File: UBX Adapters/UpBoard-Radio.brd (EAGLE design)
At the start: 32 x 36 mm, 2 parts

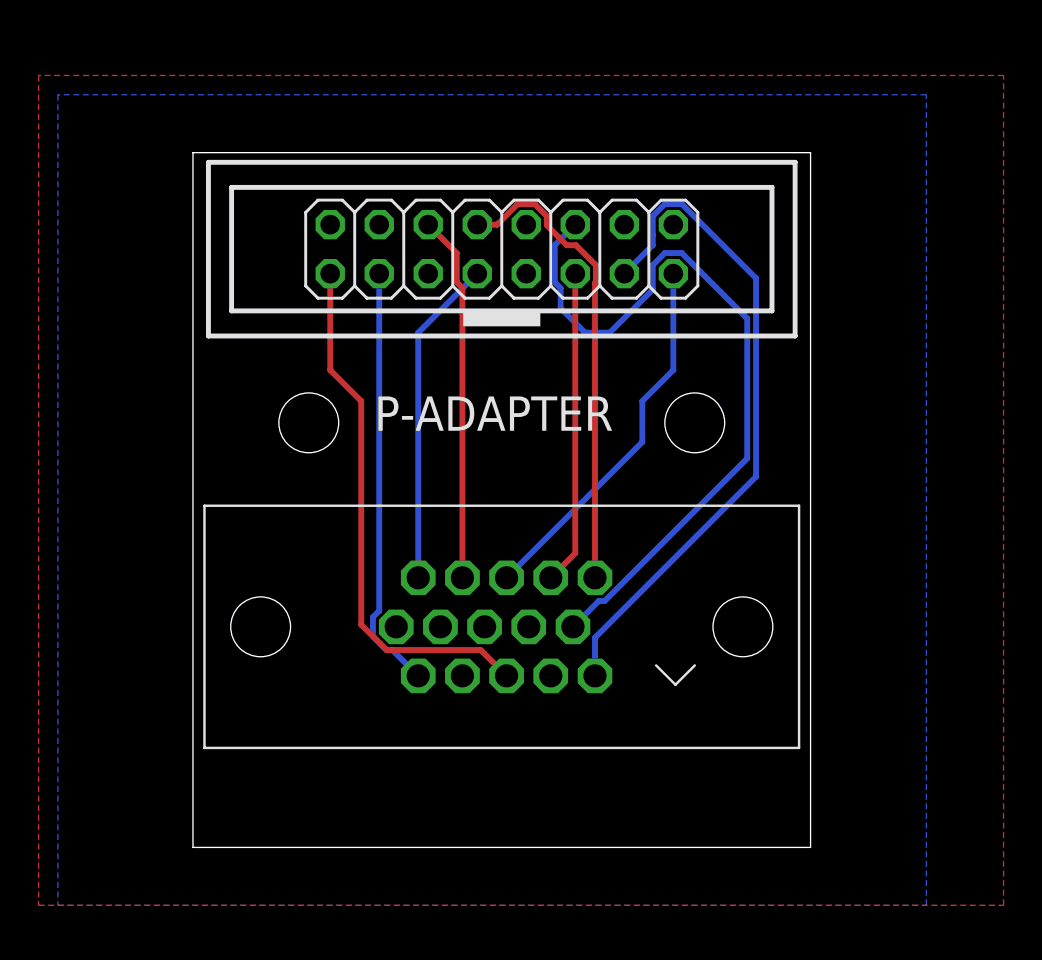
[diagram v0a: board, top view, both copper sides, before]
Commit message: created and finished upboard radio adapter
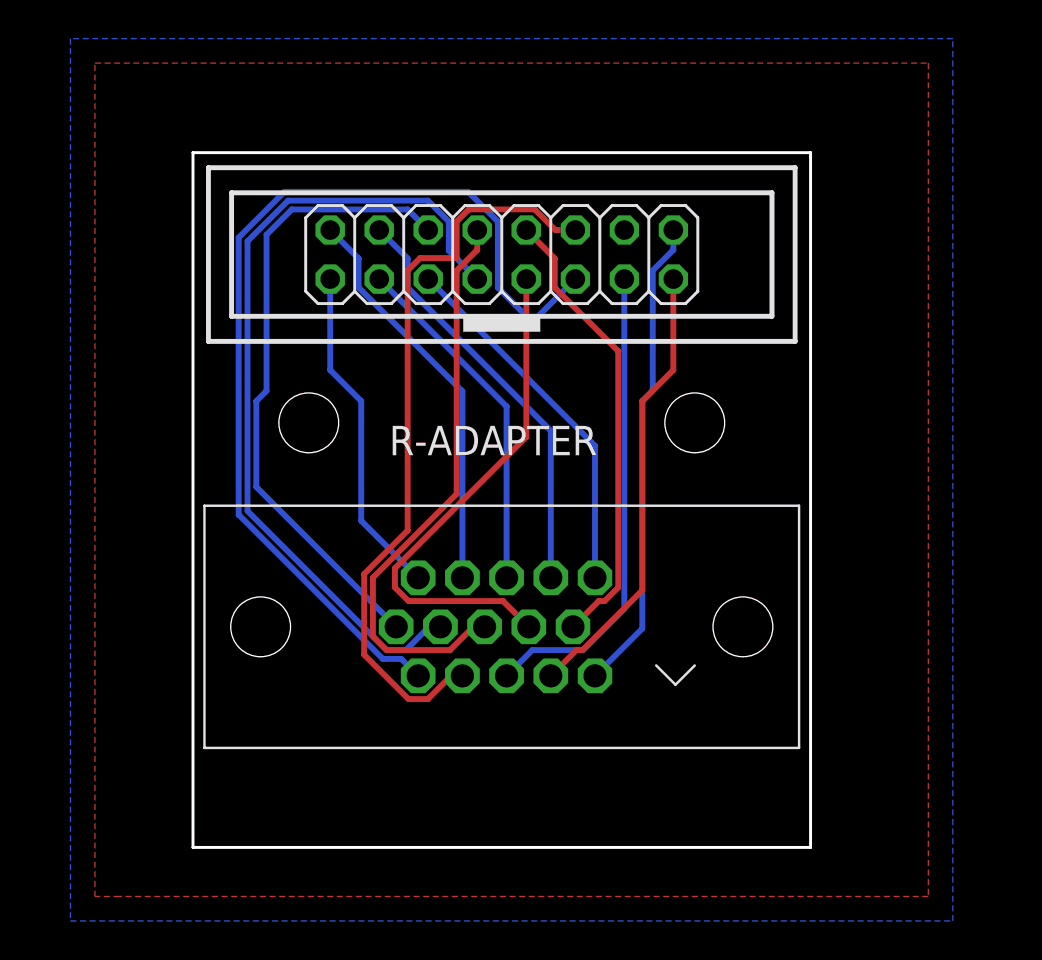
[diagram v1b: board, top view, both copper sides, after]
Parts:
- U$1: value 16POS_RIBBON -> 15POSD-SUBSLDR; device CPSS_CONNECTOR:2X08 -> CPSS_CONNECTOR:15POS-DSUBSLDR
- U$2: value 15POSD-SUBSLDR -> 16POS_RIBBON; device CPSS_CONNECTOR:15POS-DSUBSLDR -> CPSS_CONNECTOR:2X08
- moved U$1 19.6 mm to (16.0, 11.4)
- moved U$2 19.3 mm to (16.0, 30.7)
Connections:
- removed net BUSY: U$1.15, U$2.3
- removed net CONVST: U$1.13, U$2.15
- removed net CS: U$1.11, U$2.4
- removed net RESET: U$1.12, U$2.10
- new net RX: U$1.11, U$2.11
- new net RXS0: U$1.4, U$2.4
- new net SCL: U$1.10, U$2.10
- new net SDA: U$1.9, U$2.9
- new net TX: U$1.12, U$2.12
- new net TXS0: U$1.5, U$2.5
- new net XBEEATTN: U$1.14, U$2.15
- new net XBEECS: U$1.15, U$2.16
- new net XBEERESET: U$1.13, U$2.13
- net 3.3V: now also U$2.1; no longer U$2.13
- net GND: now also U$2.2; no longer U$2.12
- net HV: now also U$2.3; no longer U$2.11
- net MISO: now also U$2.6; no longer U$2.2
- net MOSI: now also U$2.7; no longer U$2.1
- net SCK: now also U$2.8; no longer U$2.5
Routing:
- net RX: track 0.00 -> 51.3 mm
- net TX: track 0.00 -> 38.9 mm
- net RESET: track 38.8 -> 0.00 mm
- net CONVST: track 34.9 -> 0.00 mm
- net SDA: track 0.00 -> 26.6 mm
- net MOSI: track 17.0 -> 42.8 mm
- net XBEECS: track 0.00 -> 24.8 mm
- net XBEERESET: track 0.00 -> 24.6 mm
- net SCL: track 0.00 -> 23.7 mm
- net XBEEATTN: track 0.00 -> 23.4 mm
- net RXS0: track 0.00 -> 21.7 mm
- net GND: track 0.00 -> 20.9 mm
- net BUSY: track 19.3 -> 0.00 mm
- net TXS0: track 0.00 -> 19.1 mm
- net CS: track 16.3 -> 0.00 mm
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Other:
- board text added: "R-ADAPTER"
- board text removed: "P-ADAPTER"
